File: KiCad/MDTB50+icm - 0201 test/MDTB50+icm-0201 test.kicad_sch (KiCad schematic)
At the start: 34 parts, among them SW1 1TS026A-1100-0550-CT, U1 ICM-45686, U2 TXS0102DQER, U3 QMC6309, U4 SSP7615-18DFR, U5 SSP7615-33DFR, X1 SX2M32.768KM20F30TNN

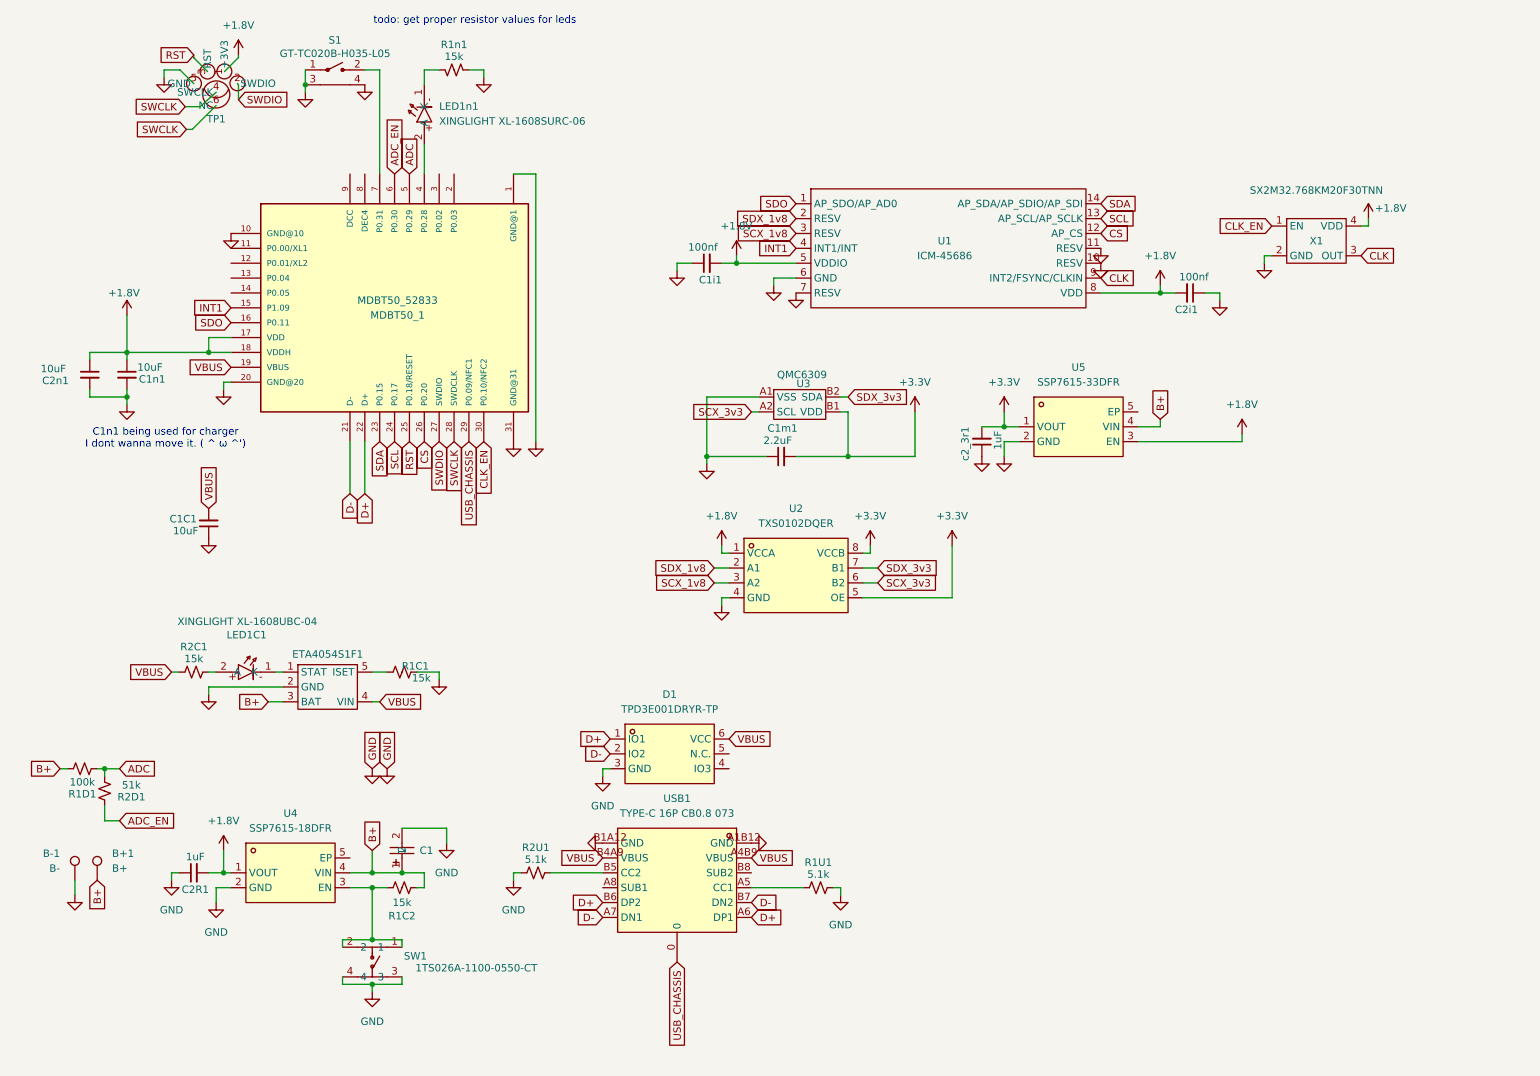
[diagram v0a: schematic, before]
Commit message: - Added 0201 version with: DCDC, RGB LED, replaced charger IC, shortened   by 2mm.
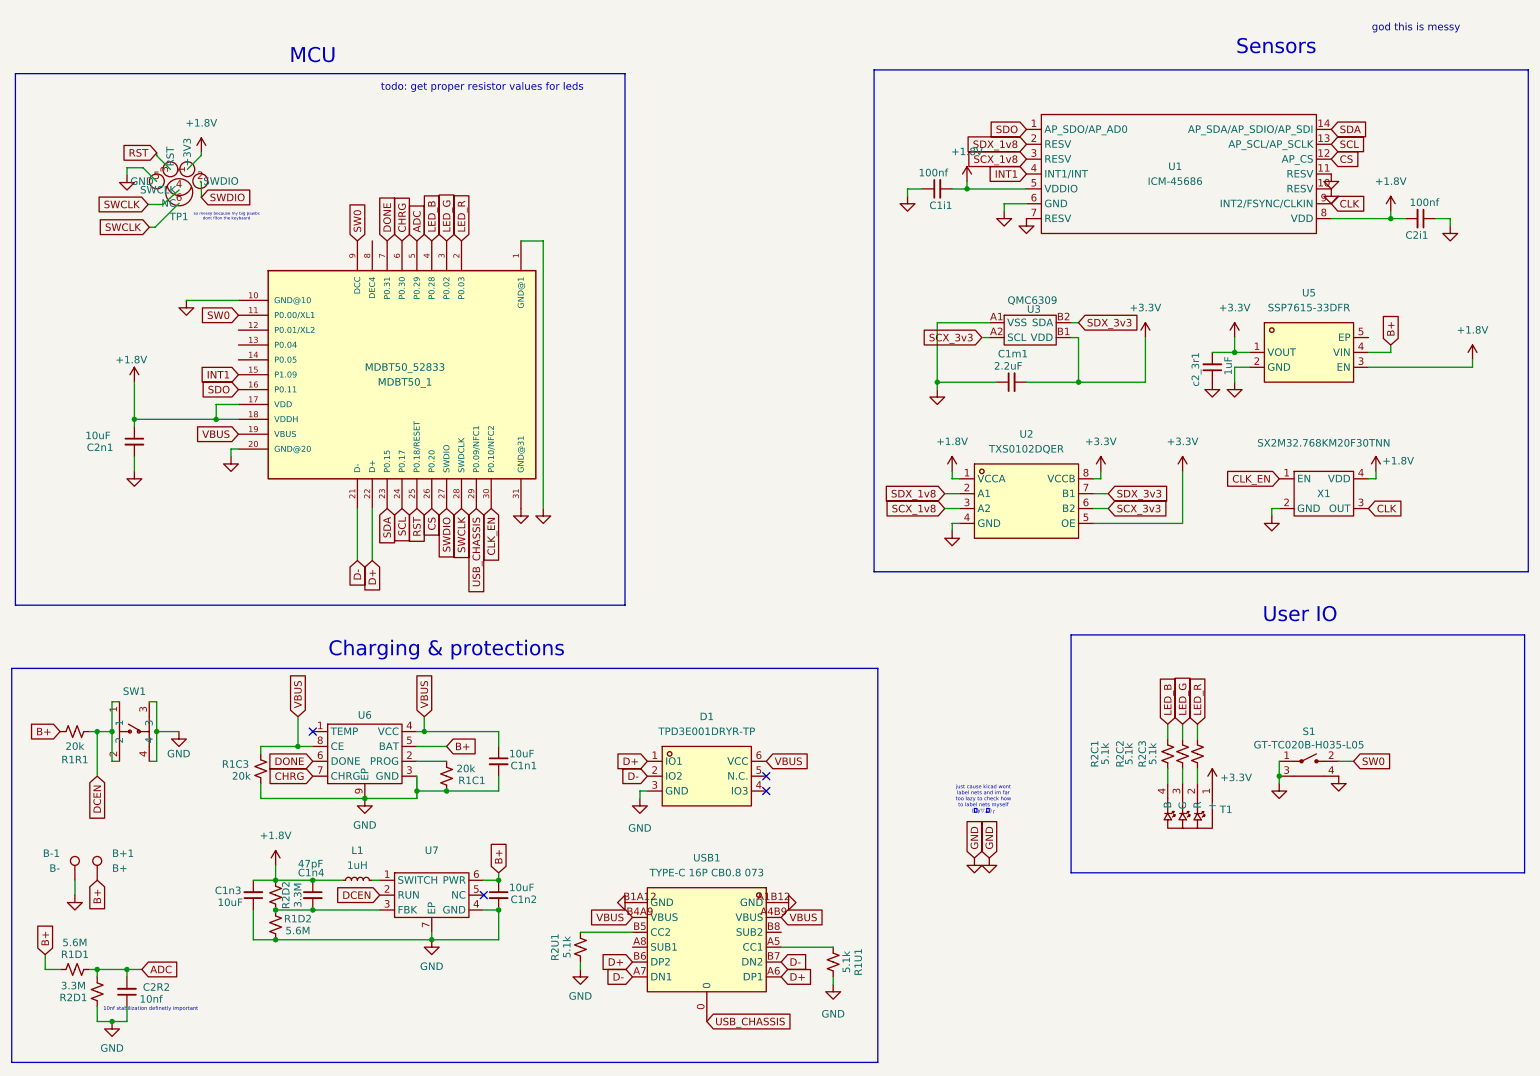
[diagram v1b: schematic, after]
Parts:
- removed C1: TAJA105K016RNJ, easyeda2kicad:CASE-A_3216, symbol easyeda2kicad:TAJA105K016RNJ
- removed C1C1: 10uF, passive_custom:C_0402_JLC, symbol Device:C_Small
- removed C2R1: 1uF, passive_custom:C_0402_JLC, symbol Device:C_Small
- removed ETA4054S1F1: ETA4054S1F1, battery_management_custom:ETA4054S2F, symbol Battery_management_custom_2:ETA4054S2F
- removed LED1C1: XINGLIGHT XL-1608UBC-04, LED_custom:XINGLIGHT XL-1608UBC-04, symbol LED_custom2:XINGLIGHT_XL-1608UBC-04
- removed LED1n1: XINGLIGHT XL-1608SURC-06, LED_custom:XINGLIGHT XL-1608UBC-04, symbol LED_custom2:XINGLIGHT_XL-1608UBC-04
- removed R1n1: 15k, passive_custom:R_0402_JLC, symbol Device:R_Small_US
- removed U4: SSP7615-18DFR, easyeda2kicad:DFN-4_L1.0-W1.0-P0.65-BL-EP, symbol easyeda2kicad:SSP7615-18DFR
- added C1n2, C1n3: 10uF, passive_custom:C_0402_JLC, symbol Device:C_Small
- added C1n4: 47pF, passive_custom:C_0201_JLC, symbol Device:C_Small
- added C2R2: 10nf, passive_custom:C_0201_JLC, symbol Device:C_Small
- added L1: 1uH, easyeda2kicad:L0603, symbol Device:L_Small
- added R1C3: 20k, passive_custom:R_0201_JLC, symbol Device:R_Small_US
- added R1D2: 5.6M, passive_custom:R_0201_JLC, symbol Device:R_Small_US
- added R2C2, R2C3: 5.1k, passive_custom:R_0201_JLC, symbol Device:R_Small_US
- added R2D2: 3.3M, passive_custom:R_0201_JLC, symbol Device:R_Small_US
- added T1: ~, easyeda2kicad:LED-ARRAY-SMD_4P-L0.80-W0.80-BR, symbol LED_custom2:MHPA0808RGBDT
- added U6: ~, easyeda2kicad:DFN-8_L2.0-W2.0-P0.50-TL-EP1.6, symbol easyeda2kicad:LGS4056HDA
- added U7: ~, easyeda2kicad:DFN-6_L1.5-W1.5-P0.50-BL-EP1.0, symbol easyeda2kicad:EA8103DHR
- C1i1, C1m1, C2i1, c2_3r1: footprint passive_custom:C_0402_JLC -> passive_custom:C_0201_JLC
- R1C1: value 15k -> 20k; footprint passive_custom:R_0402_JLC -> passive_custom:R_0201_JLC
- R1D1: value 100k -> 5.6M; footprint passive_custom:R_0402_JLC -> passive_custom:R_0201_JLC
- R1R1: renamed from R1C2; value 15k -> 20k; footprint passive_custom:R_0402_JLC -> passive_custom:R_0201_JLC
- R1U1, R2U1: footprint passive_custom:R_0402_JLC -> passive_custom:R_0201_JLC
- R2C1: value 15k -> 5.1k; footprint passive_custom:R_0402_JLC -> passive_custom:R_0201_JLC
- R2D1: value 51k -> 3.3M; footprint passive_custom:R_0402_JLC -> passive_custom:R_0201_JLC
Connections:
- net +1.8V: now also C1n3.2, C1n4.1, L1.1, R2D2.2; no longer C1n1.1
- net +3.3V: now also T1.1 (+)
- net ADC: now also C2R2.2
- net B+: now also R1R1.1, C1n2.1, U6.5 (BAT), U7.6 (PWR); no longer R1R1.2
- net GND: now also R2D1.1, C1n2.2, C1n3.1, C2R2.1, R1C3.1, R1D2.1, U6.3 (GND), U6.9 (EP), U7.4 (GND), U7.7 (EP)
- net VBUS: now also C1n1.1, R1C3.2, U6.4 (VCC), U6.8 (CE); no longer R2C1.1
- net LED_B: now reaches R2C1.2
- net LED_B: now also MDBT50_1.4 (P0.28)
- net DCEN: now reaches SW1.1, SW1.2
- net DCEN: now also R1R1.2, U7.2 (RUN); no longer R1R1.1
- net SW0: now reaches MDBT50_1.11 (P0.00/XL1)
- net SW0: now also MDBT50_1.9 (DCC), S1.2
- net LED_R: now reaches MDBT50_1.2 (P0.03)
- net LED_R: now also R2C3.2
- net LED_G: now reaches MDBT50_1.3 (P0.02)
- net LED_G: now also R2C2.2
- net DONE: now reaches MDBT50_1.7 (P0.31)
- net DONE: now also U6.6 (DONE); no longer S1.2
- net at R1C1.1: now also U6.2 (PROG)
- net ADC_EN renamed CHRG
- net CHRG: now also U6.7 (CHRG); no longer R2D1.1
- new net: R2C1.1, T1.4 (B)
- new net: C1n4.2, R1D2.2, R2D2.1, U7.3 (FBK)
- new net: R2C2.1, T1.3 (G)
- new net: L1.2, U7.1 (SWITCH)
- new net: R2C3.1, T1.2 (R)
- no-connect marks 0 -> 4
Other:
- note added: "10nf stabilization definetly important"
- note added: "Charging & protections"
- note added: "MCU"
- note added: "Sensors"
- note added: "User IO"
- note added: "god this is messy"
- note added: "just cause kicad wont label nets and im far too lazy to check how to label nets myself (￣y▽,￣)╭"
- note added: "so messy because my big pawbs dont fiton the keybaord"
- note removed: "C1n1 being used for charger I dont wanna move it. ( ^ ω ^')"
- moved on the sheet: C1i1, C1m1, C2i1, C2n1, D1, MDBT50_1, R1D1, R1R1, R1U1, R2D1, R2U1, SW1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
